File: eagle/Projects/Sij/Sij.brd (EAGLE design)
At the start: 100 x 80 mm, 9 parts, among them U1 ATMEGA2560AU

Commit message: ajouté des pièces pour digikey
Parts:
- added U2: BQ76925_PW_20, TI:PW20
- added U3: LM1085_KTT_3, TI:KTT3
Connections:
- new net BAT: U2.2
- new net VSS: U2.10
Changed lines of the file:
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@@
 <attribute name="PROD_ID" value="CAP-07876" x="54.61" y="17.78" size="1.778" layer="27" display="off"/>
+</element>
+<element name="U2" library="TI" package="PW20" value="BQ76925_PW_20" x="5.08" y="-5.08">
+<attribute name="GENERIC_PART_NUMBER" value="BQ76925" x="5.08" y="-5.08" size="1.778" layer="27" display="off"/>
+<attribute name="PACKAGE_DESIGNATOR" value="PW" x="5.08" y="-5.08" size="1.778" layer="27" display="off"/>
+<attribute name="MANUFACTURER" value="Texas Instruments" x="5.08" y="-5.08" size="1.778" layer="27" display="off"/>
+<attribute name="DESCRIPTION" value="Analog Front End for 3 to 6 Series Lithium-Ion Cells" x="5.08" y="-5.08" size="1.778" layer="27" display="off"/>
+<attribute name="VENDOR" value="Texas Instruments" x="5.08" y="-5.08" size="1.778" layer="27" display="off"/>
+<attribute name="INDUSTRY_STD_PKG_TYPE" value="TSSOP" x="5.08" y="-5.08" size="1.778" layer="27" display="off"/>
+<attribute name="FAMILY_NAME" value="LITHIUM ION PROTECTION" x="5.08" y="-5.08" size="1.778" layer="27" display="off"/>
+<attribute name="MANUFACTURER_PART_NUMBER" value="bq76925_pw_20" x="5.08" y="-5.08" size="1.778" layer="27" display="off"/>
+<attribute name="PIN_COUNT" value="20" x="5.08" y="-5.08" size="1.778" layer="27" display="off"/>
+<attribute name="DATASHEETURL" value="http://www.ti.com/lit/gpn/BQ76925" x="5.08" y="-5.08" size="1.778" layer="27" display="off"/>
+</element>
+<element name="U3" library="TI" package="KTT3" value="LM1085_KTT_3" x="-6.35" y="3.81">
+<attribute name="VENDOR" value="Texas Instruments" x="-6.35" y="3.81" size="1.778" layer="27" display="off"/>
+<attribute name="MANUFACTURER_PART_NUMBER" value="lm1085_ktt_3" x="-6.35" y="3.81" size="1.778" layer="27" display="off"/>
 </element>
 </elements>
@@
 <wire x1="45.3" y1="17.78" x2="46.99" y2="22.86" width="0" layer="19" extent="1-1"/>
 </signal>
+<signal name="BAT">
+<contactref element="U2" pad="2"/>
+</signal>
+<signal name="VSS">
+<contactref element="U2" pad="10"/>
+</signal>
 </signals>

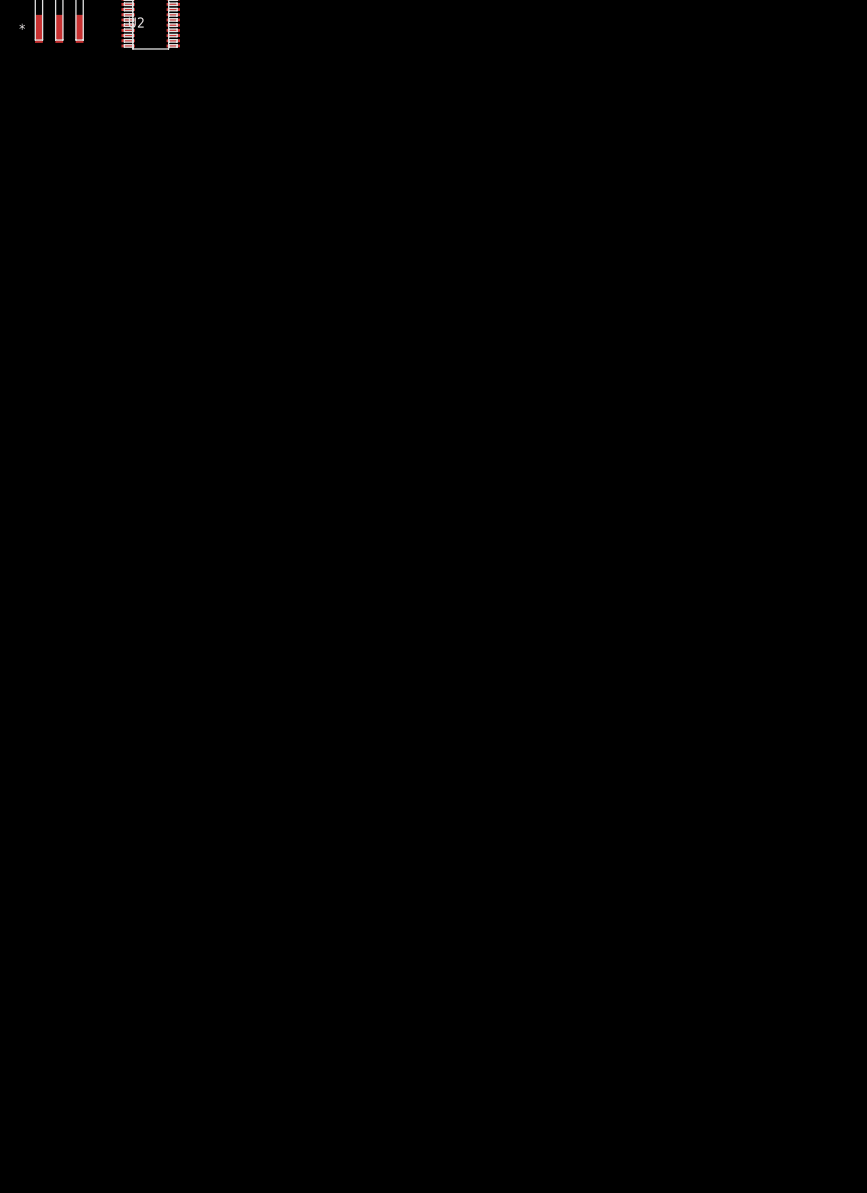
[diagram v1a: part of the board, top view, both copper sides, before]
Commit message: ajouté des bibliothèques de composantes, modifié beaucoup le schematic du pcb et ajouté des listes d'épicerie
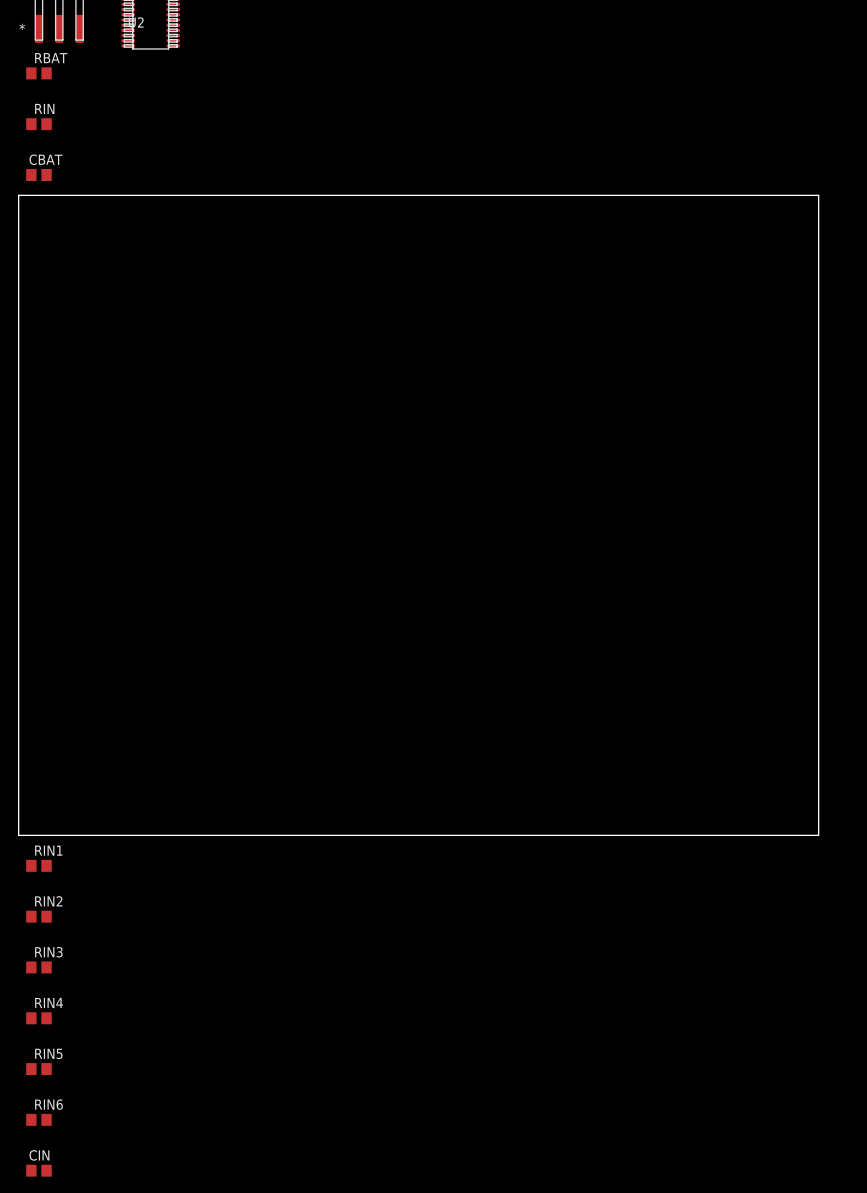
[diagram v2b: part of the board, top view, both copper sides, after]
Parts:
- added CBAT: 10u, rcl:C0805
- added CIN: cco, rcl:C0805
- added RBAT, RIN1, RIN2, RIN3, RIN4, RIN5, RIN6: 100, rcl:R0805
- added RIN: cco, rcl:R0805
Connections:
- removed net BAT: U2.2
- new net N$10: RIN1.2, U2.8
- new net N$11: CIN.1, RIN.2, U2.9
- new net N$12: RIN4.2, U2.5
- new net N$17: RIN6.2, U2.3
- new net N$18: RIN5.2, U2.4
- new net N$7: RIN3.2, U2.6
- new net N$8: CBAT.1, RBAT.2, U2.2
- new net N$9: RIN2.2, U2.7
- net GND: now also CBAT.2
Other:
- board size 100 x 80 mm -> 111.4 x 186.7 mm
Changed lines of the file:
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@@
 <wire x1="100" y1="80" x2="0" y2="80" width="0" layer="20"/>
 <wire x1="0" y1="80" x2="0" y2="0" width="0" layer="20"/>
+<wire x1="-11.43" y1="-106.68" x2="88.57" y2="-106.68" width="0" layer="20"/>
+<wire x1="88.57" y1="-106.68" x2="88.57" y2="-26.68" width="0" layer="20"/>
+<wire x1="88.57" y1="-26.68" x2="-11.43" y2="-26.68" width="0" layer="20"/>
+<wire x1="-11.43" y1="-26.68" x2="-11.43" y2="-106.68" width="0" layer="20"/>
 </plain>
 <attributes>
@@
 <attribute name="MANUFACTURER_PART_NUMBER" value="lm1085_ktt_3" x="-6.35" y="3.81" size="1.778" layer="27" display="off"/>
 </element>
+<element name="RBAT" library="rcl" package="R0805" value="100" x="-8.89" y="-11.43"/>
+<element name="RIN" library="rcl" package="R0805" value="cco" x="-8.89" y="-17.78"/>
+<element name="CBAT" library="rcl" package="C0805" value="10u" x="-8.89" y="-24.13"/>
+<element name="RIN1" library="rcl" package="R0805" value="100" x="-8.89" y="-110.49"/>
+<element name="RIN2" library="rcl" package="R0805" value="100" x="-8.89" y="-116.84"/>
+<element name="RIN3" library="rcl" package="R0805" value="100" x="-8.89" y="-123.19"/>
+<element name="RIN4" library="rcl" package="R0805" value="100" x="-8.89" y="-129.54"/>
+<element name="RIN5" library="rcl" package="R0805" value="100" x="-8.89" y="-135.89"/>
+<element name="RIN6" library="rcl" package="R0805" value="100" x="-8.89" y="-142.24"/>
+<element name="CIN" library="rcl" package="C0805" value="cco" x="-8.89" y="-148.59"/>
 </elements>
 <signals>
@@
 <contactref element="C1" pad="1"/>
 <contactref element="C2" pad="1"/>
+<contactref element="CBAT" pad="2"/>
 <wire x1="25.4" y1="41.91" x2="44.07" y2="40.37" width="0" layer="19" extent="1-1"/>
-<wire x1="43.6" y1="17.78" x2="25.4" y2="41.91" width="0" layer="19" extent="1-1"/>
+<wire x1="43.6" y1="17.78" x2="44.07" y2="40.37" width="0" layer="19" extent="1-1"/>
 <wire x1="53.76" y1="17.78" x2="43.6" y2="17.78" width="0" layer="19" extent="1-1"/>
+<wire x1="-7.94" y1="-24.13" x2="43.6" y2="17.78" width="0" layer="19" extent="1-1"/>
 </signal>
 <signal name="GND1">
@@
 <contactref element="U1" pad="26"/>
 <contactref element="ESC1" pad="8"/>
-<wire x1="46.07" y1="31.37" x2="5.08" y2="5.08" width="0" layer="19" extent="1-1"/>
+<wire x1="5.08" y1="5.08" x2="46.07" y2="31.37" width="0" layer="19" extent="1-1"/>
 </signal>
 <signal name="PWMB3">
 <contactref element="U1" pad="25"/>
 <contactref element="ESC1" pad="7"/>
-<wire x1="44.07" y1="33.37" x2="2.54" y2="5.08" width="0" layer="19" extent="1-1"/>
+<wire x1="2.54" y1="5.08" x2="44.07" y2="33.37" width="0" layer="19" extent="1-1"/>
 </signal>
 <signal name="PWMB2">
@@
 <contactref element="U1" pad="23"/>
 <contactref element="ESC1" pad="5"/>
-<wire x1="44.07" y1="34.37" x2="2.54" y2="7.62" width="0" layer="19" extent="1-1"/>
+<wire x1="2.54" y1="7.62" x2="44.07" y2="34.37" width="0" layer="19" extent="1-1"/>
 </signal>
 <signal name="PWME3">
@@
 <contactref element="U1" pad="18"/>
 <contactref element="ESC4" pad="7"/>
-<wire x1="95.25" y1="69.85" x2="44.07" y2="36.87" width="0" layer="19" extent="1-1"/>
+<wire x1="44.07" y1="36.87" x2="95.25" y2="69.85" width="0" layer="19" extent="1-1"/>
 </signal>
 <signal name="PWMH3">
 <contactref element="U1" pad="17"/>
 <contactref element="ESC4" pad="6"/>
-<wire x1="97.79" y1="72.39" x2="44.07" y2="37.37" width="0" layer="19" extent="1-1"/>
+<wire x1="44.07" y1="37.37" x2="97.79" y2="72.39" width="0" layer="19" extent="1-1"/>
 </signal>
 <signal name="PWMH2">
 <contactref element="U1" pad="16"/>
 <contactref element="ESC4" pad="5"/>
-<wire x1="95.25" y1="72.39" x2="44.07" y2="37.87" width="0" layer="19" extent="1-1"/>
+<wire x1="44.07" y1="37.87" x2="95.25" y2="72.39" width="0" layer="19" extent="1-1"/>
 </signal>
 <signal name="PWMH1">
 <contactref element="U1" pad="15"/>
 <contactref element="ESC4" pad="4"/>
-<wire x1="97.79" y1="74.93" x2="44.07" y2="38.37" width="0" layer="19" extent="1-1"/>
+<wire x1="44.07" y1="38.37" x2="97.79" y2="74.93" width="0" layer="19" extent="1-1"/>
 </signal>
 <signal name="PWML1">
 <contactref element="U1" pad="38"/>
 <contactref element="ESC3" pad="4"/>
-<wire x1="97.79" y1="10.16" x2="52.07" y2="31.37" width="0" layer="19" extent="1-1"/>
+<wire x1="52.07" y1="31.37" x2="97.79" y2="10.16" width="0" layer="19" extent="1-1"/>
 </signal>
 <signal name="PWML2">
 <contactref element="U1" pad="39"/>
 <contactref element="ESC3" pad="5"/>
-<wire x1="95.25" y1="7.62" x2="52.57" y2="31.37" width="0" layer="19" extent="1-1"/>
+<wire x1="52.57" y1="31.37" x2="95.25" y2="7.62" width="0" layer="19" extent="1-1"/>
 </signal>
 <signal name="PWML3">
 <contactref element="U1" pad="40"/>
 <contactref element="ESC3" pad="6"/>
-<wire x1="97.79" y1="7.62" x2="53.07" y2="31.37" width="0" layer="19" extent="1-1"/>
+<wire x1="53.07" y1="31.37" x2="97.79" y2="7.62" width="0" layer="19" extent="1-1"/>
 </signal>
 <signal name="PWMG1">
@@
 <wire x1="45.3" y1="17.78" x2="46.99" y2="22.86" width="0" layer="19" extent="1-1"/>
 </signal>
-<signal name="BAT">
-<contactref element="U2" pad="2"/>
-</signal>
 <signal name="VSS">
 <contactref element="U2" pad="10"/>
 </signal>
+<signal name="N$8">
+<contactref element="CBAT" pad="1"/>
+<contactref element="RBAT" pad="2"/>
+<contactref element="U2" pad="2"/>
+<wire x1="-7.94" y1="-11.43" x2="-9.84" y2="-24.13" width="0" layer="19" extent="1-1"/>
+<wire x1="2.2606" y1="-2.805" x2="-7.94" y2="-11.43" width="0" layer="19" extent="1-1"/>
+</signal>
+<signal name="N$17">
+<contactref element="U2" pad="3"/>
+<contactref element="RIN6" pad="2"/>
+<wire x1="2.2606" y1="-3.455" x2="-7.94" y2="-142.24" width="0" layer="19" extent="1-1"/>
+</signal>
+<signal name="N$18">
+<contactref element="U2" pad="4"/>
+<contactref element="RIN5" pad="2"/>
+<wire x1="2.2606" y1="-4.105" x2="-7.94" y2="-135.89" width="0" layer="19" extent="1-1"/>
+</signal>
+<signal name="N$7">
+<contactref element="U2" pad="6"/>
+<contactref element="RIN3" pad="2"/>
+<wire x1="2.2606" y1="-5.404996875" x2="-7.94" y2="-123.19" width="0" layer="19" extent="1-1"/>
+</signal>
+<signal name="N$9">
+<contactref element="U2" pad="7"/>
+<contactref element="RIN2" pad="2"/>
+<wire x1="2.2606" y1="-6.055" x2="-7.94" y2="-116.84" width="0" layer="19" extent="1-1"/>
+</signal>
+<signal name="N$10">
+<contactref element="U2" pad="8"/>
+<contactref element="RIN1" pad="2"/>
+<wire x1="2.2606" y1="-6.704996875" x2="-7.94" y2="-110.49" width="0" layer="19" extent="1-1"/>
+</signal>
+<signal name="N$11">
+<contactref element="U2" pad="9"/>
+<contactref element="RIN" pad="2"/>
+<contactref element="CIN" pad="1"/>
+<wire x1="-7.94" y1="-17.78" x2="-9.84" y2="-148.59" width="0" layer="19" extent="1-1"/>
+<wire x1="2.2606" y1="-7.355" x2="-7.94" y2="-17.78" width="0" layer="19" extent="1-1"/>
+</signal>
+<signal name="N$12">
+<contactref element="U2" pad="5"/>
+<contactref element="RIN4" pad="2"/>
+<wire x1="2.2606" y1="-4.755" x2="-7.94" y2="-129.54" width="0" layer="19" extent="1-1"/>
+</signal>
 </signals>

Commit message: modifié le TODO
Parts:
- added BAT+, BAT-: AWG_10_HOLE_PAD, custom_parts:AWG10_HOLE_PAD
- added CIN1, CIN2, CIN3, CIN4, CIN5, CIN6, COUT2, CREF: 1.0uF, SparkFun-Capacitors:0603-CAP
- added CIN_1085: 10uF, SparkFun-Capacitors:0805
- added CIN_7805: 0.22uF, SparkFun-Capacitors:0603-CAP
- added COUT: 0.1u, SparkFun-Capacitors:0603-CAP
- added COUT_1085: 10uF, SparkFun-Capacitors:1206
- added COUT_7805: 0.1uF, SparkFun-Capacitors:0603-CAP
- added CSENSE: 0.1u, rcl:C0805
- added CV3P3: 4.7uF, SparkFun-Capacitors:0603-CAP
- added ESC1+, ESC1-, ESC2+, ESC2-, ESC3+, ESC3-, ESC4+, ESC4-: BULLET_PAD, custom_parts:4.5MM_SQUARE
- added ESC1_PWM, ESC2_PWM, ESC3_PWM, ESC4_PWM, JUMP_3_CELL, JUMP_4_CELL, JUMP_5_CELL, JUMP_PWR_BAT, JUMP_PWR_PROG: (no value), SparkFun-Connectors:1X02
- added J1: (no value), SparkFun-Connectors:1X06_FEMALE_LOCK.010
- added R1: 121, resistor:R0603
- added R2: adj, resistor:R0603
- added RSENSE: 1m, resistor:R1206
- added RSENSEN, RSENSEP: 1K, resistor:R0603
- added U$1: 7_PIN_JST-XH, JST-XH_HEADERS:7_PIN_JST-XH
- added U4: LM7805, TI:KTT3
- CBAT: value 10u -> 10uF; device rcl:C0805 -> SparkFun-Capacitors:0805
- CIN: value cco -> 1.0uF; device rcl:C0805 -> SparkFun-Capacitors:0603-CAP
- RBAT, RIN1, RIN2, RIN3, RIN4, RIN5, RIN6: device rcl:R0805 -> resistor:R0603
- RIN: value cco -> 100; device rcl:R0805 -> resistor:R0603
- moved U3 24.5 mm to (16.5, 12.7)
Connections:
- removed net GND1: U1.32
- removed net GND2: U1.62
- removed net GND3: U1.81
- removed net VCC1: U1.31
- removed net VCC2: U1.61
- removed net VCC3: U1.80
- removed net VSS: U2.10
- new net GND-ISO: ESC1-.IN, ESC2-.IN, ESC3-.IN, ESC4-.IN, RSENSE.1, RSENSEN.1
- new net N$13: COUT_7805.1, JUMP_PWR_BAT.2, U4.3
- new net N$14: BAT-.P$1, RSENSE.2, RSENSEP.1
- new net N$15: CSENSE.1, RSENSEN.2, U2.11
- new net N$16: CSENSE.2, RSENSEP.2, U2.12
- new net N$19: U2.18
- new net N$20: U2.13
- new net N$21: COUT2.1, U2.14
- new net N$22: COUT.1, U2.15
- new net N$23: RIN1.1, U$1.P$2
- new net N$24: CREF.1, U2.17
- new net N$25: U2.19
- new net N$26: CV3P3.1, U2.20
- new net N$27: RIN2.1, U$1.P$3
- new net N$28: JUMP_3_CELL.1, RIN3.1, U$1.P$4
- new net N$29: JUMP_3_CELL.2, JUMP_4_CELL.1, RIN4.1, U$1.P$5
- new net N$30: JUMP_4_CELL.2, JUMP_5_CELL.1, RIN5.1, U$1.P$6
- new net N$31: ICSP.2, JUMP_PWR_PROG.1
- new net N$32: COUT_1085.1, J1.1, J1.2, J1.3, J1.4, J1.5, J1.6, R1.1, U3.2, U3.4
- new net N$33: R1.2, R2.2, U3.3
- new net V_BATT: BAT+.P$1, CIN_1085.1, CIN_7805.1, ESC1+.IN, ESC2+.IN, ESC3+.IN, ESC4+.IN, JUMP_5_CELL.2, RBAT.1, RIN6.1, U$1.P$7, U3.1, U4.1
- net GND: now also CIN.2, CIN1.2, CIN2.2, CIN3.2, CIN4.2, CIN5.2, CIN6.2, CIN_1085.2, CIN_7805.2, COUT.2, COUT2.2, COUT_1085.2, COUT_7805.2, CREF.2, CV3P3.2, ESC1_PWM.2, ESC2_PWM.2, ESC3_PWM.2, ESC4_PWM.2, R2.1, RIN.1, U$1.P$1, U1.32, U1.62, U1.81, U2.10, U4.2, U4.4
- net N$10: now also CIN1.1
- net N$12: now also CIN4.1
- net N$17: now also CIN6.1
- net N$18: now also CIN5.1
- net N$7: now also CIN3.1
- net N$8: now also U2.1
- net N$9: now also CIN2.1
- net PWMH1: now also ESC1_PWM.1, ESC4_PWM.1, U1.18
- net PWMH2: now also ESC3_PWM.1
- net PWMH3: now also ESC2_PWM.1
- net PWMH4: no longer U1.18
- net VCC: now also JUMP_PWR_BAT.1, JUMP_PWR_PROG.2, U1.31, U1.61, U1.80; no longer ICSP.2
